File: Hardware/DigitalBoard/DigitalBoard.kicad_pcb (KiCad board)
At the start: 2 copper layers, 20 parts, among them P1 IN-PORT0, P2 IN-PORT1, P3 CONN_5, U1 TCA9535

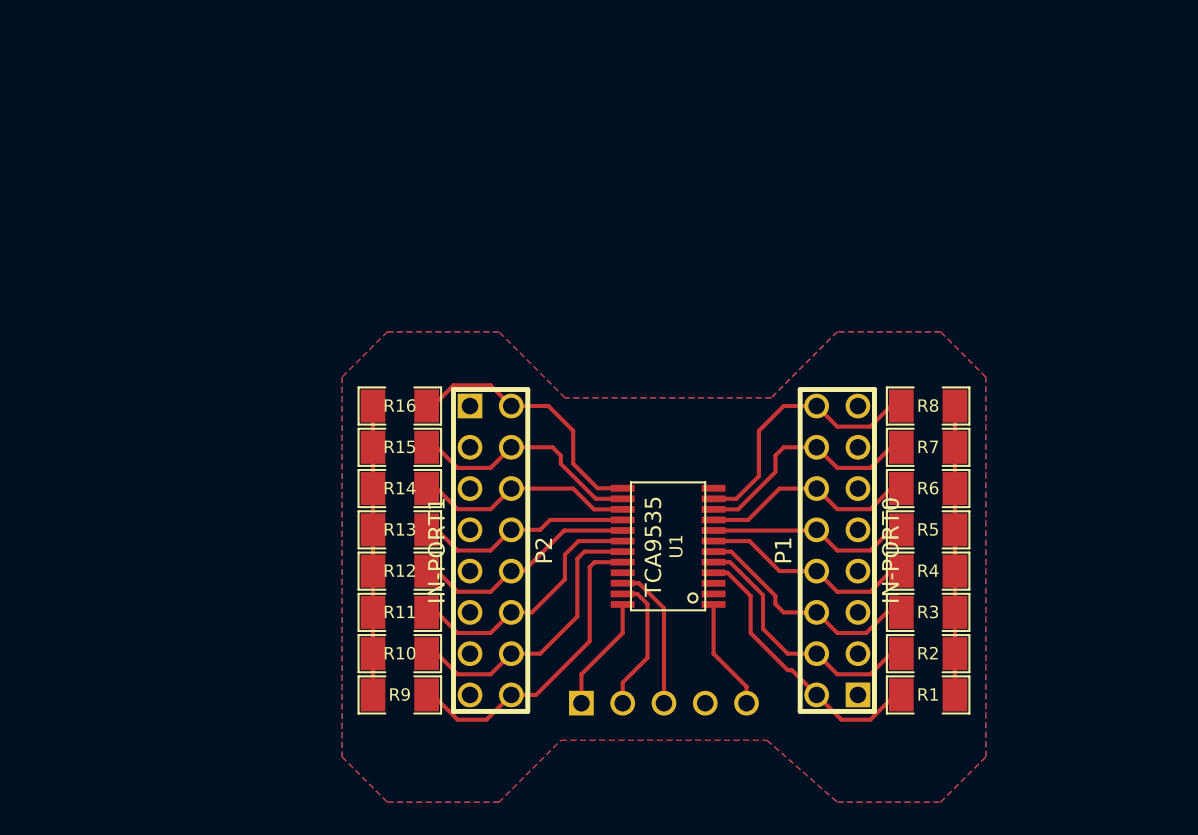
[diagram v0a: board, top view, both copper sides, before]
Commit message: Updated PCB to make it more DIY friendly Changed Vsense pin to A3 Added Design Folder
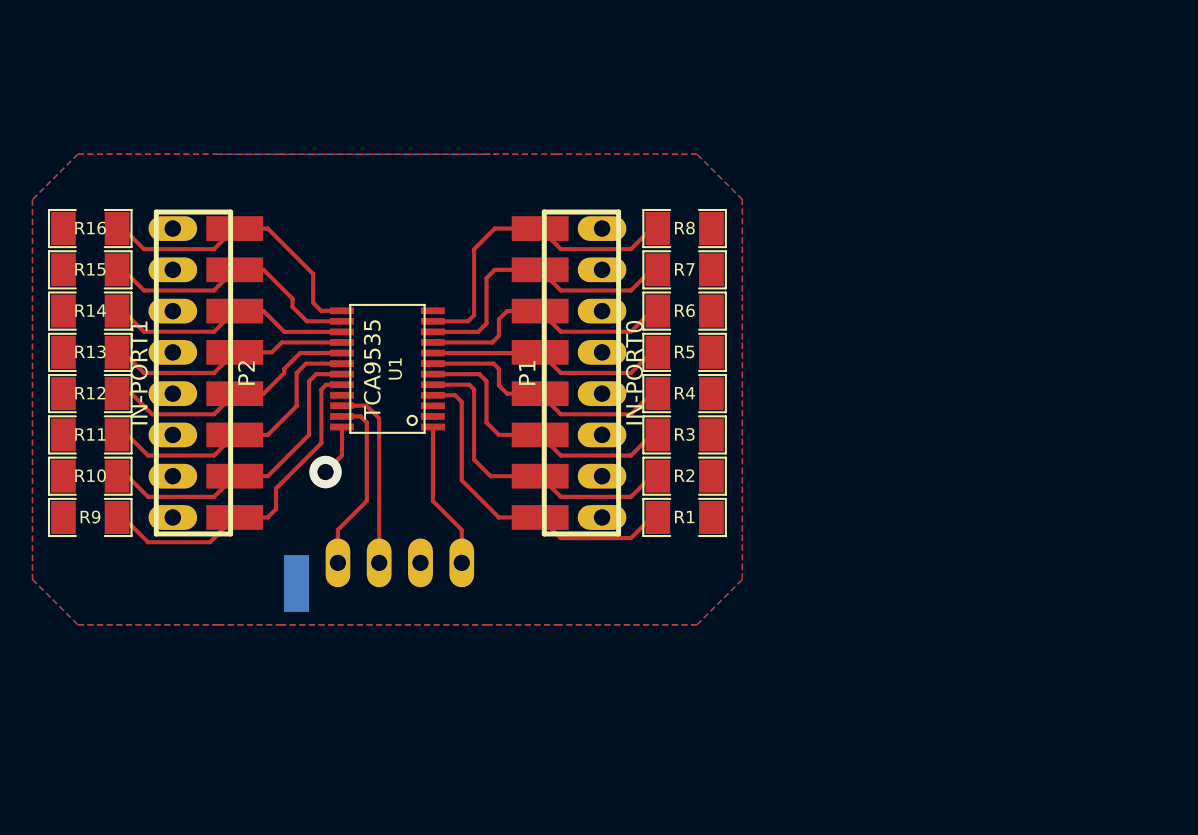
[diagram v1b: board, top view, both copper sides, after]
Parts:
- P1, P2: footprint pin_array_8x2 -> pin_array_8x2_MIXED2
- P3: footprint PIN_ARRAY_5x1 -> PIN_ARRAY_5x1_MIXED_INV
- moved R13 22.0 mm to (31.8, 42.7)
- moved R14 22.0 mm to (31.8, 40.1)
- moved R15 22.0 mm to (31.8, 37.6)
- moved R10 22.0 mm to (31.8, 50.3)
- moved R11 22.0 mm to (31.8, 47.8)
- moved R12 22.0 mm to (31.8, 45.2)
- moved R16 22.0 mm to (31.8, 35.1)
- moved R9 22.0 mm to (31.8, 52.8)
- moved P2 21.3 mm to (38.1, 43.9)
- moved U1 20.4 mm to (50.0, 43.7)
- moved P3 19.5 mm to (49.5, 55.6)
- moved P1 19.2 mm to (62.0, 43.9)
- moved R1 18.5 mm to (68.3, 52.8)
- moved R2 18.5 mm to (68.3, 50.3)
- moved R3 18.5 mm to (68.3, 47.8)
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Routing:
- net GND: track 35.6 -> 0.00 mm
- net +5V: track 7.13 -> 3.19 mm, vias 0 -> 1
- net N-000003: track 16.2 -> 19.8 mm
- net N-0000021: track 17.3 -> 20.8 mm
- net N-000002: track 14.5 -> 17.9 mm
- net N-0000018: track 14.8 -> 18.1 mm
- net N-0000017: track 16.6 -> 19.6 mm
- net N-000004: track 13.4 -> 16.3 mm
- net N-0000020: track 13.4 -> 16.3 mm
- net SDA: track 8.52 -> 11.1 mm
- net SCL: track 9.02 -> 11.5 mm
- net N-0000019: track 12.6 -> 14.9 mm
- net DIGI_INT: track 6.92 -> 9.10 mm
- net N-0000014: track 15.8 -> 17.9 mm
- net N-0000015: track 14.1 -> 16.1 mm
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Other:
- net class Default: via_dia 0.889 -> 2; via_drill 0.635 -> 1

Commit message: * Updating PCB to more rectangular + Caps + On/Off Switch * Disabling Digital Breakout board for now
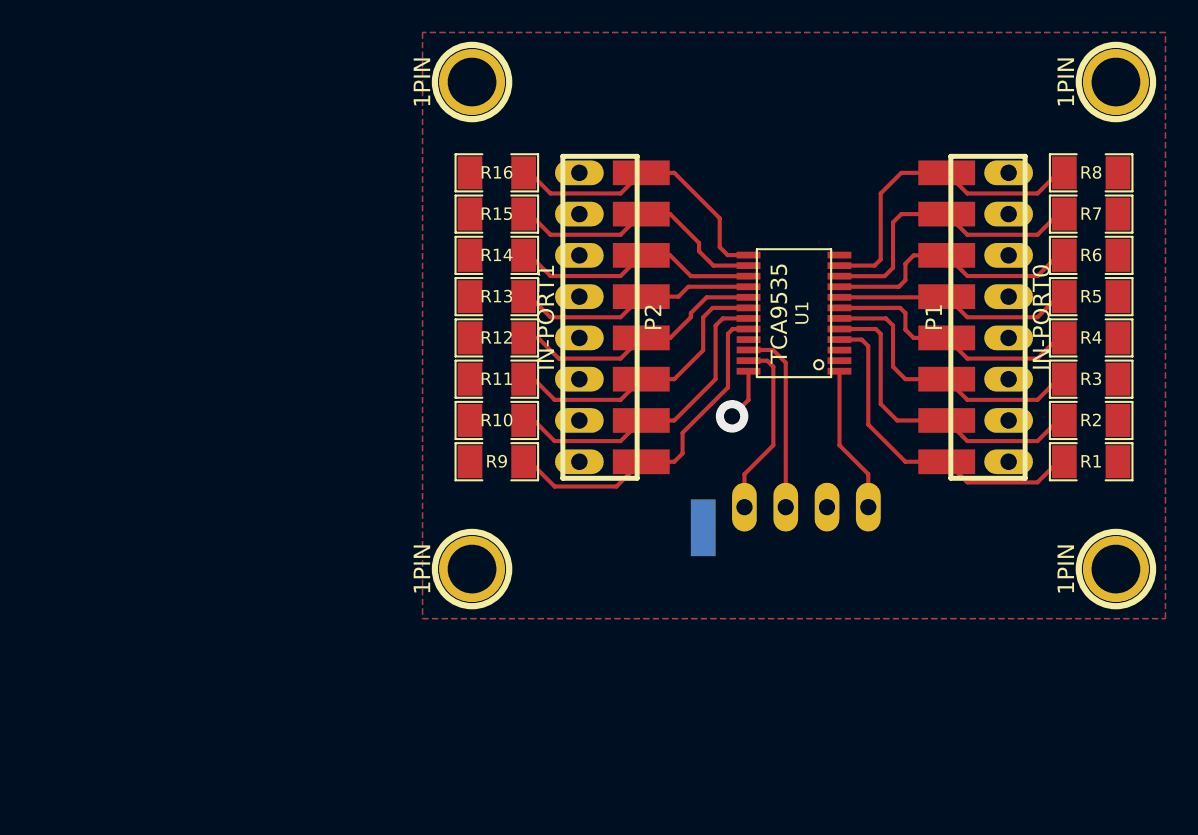
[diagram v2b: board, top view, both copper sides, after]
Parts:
- added 1PIN: P***, 1pin, F.Cu at (55.2, 26.0)
- added 1PIN: P***, 1pin, F.Cu at (94.9, 26.0)
- added 1PIN: P***, 1pin, F.Cu at (94.9, 56.0)
- added 1PIN: P***, 1pin, F.Cu at (55.2, 56.0)
- moved P1 25.3 mm to (87.0, 40.5)
- moved P3 25.3 mm to (74.5, 52.2)
- moved R1 25.3 mm to (93.3, 49.4)
- moved R2 25.3 mm to (93.3, 46.9)
- moved R3 25.3 mm to (93.3, 44.3)
- moved R4 25.3 mm to (93.3, 41.8)
- moved R5 25.3 mm to (93.3, 39.2)
- moved R6 25.3 mm to (93.3, 36.7)
- moved R7 25.3 mm to (93.3, 34.2)
- moved R8 25.3 mm to (93.3, 31.6)
- moved U1 25.3 mm to (75.1, 40.3)
- moved P2 25.3 mm to (63.1, 40.5)
- moved R10 25.3 mm to (56.8, 46.9)
- moved R11 25.3 mm to (56.8, 44.3)
- moved R12 25.3 mm to (56.8, 41.8)
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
